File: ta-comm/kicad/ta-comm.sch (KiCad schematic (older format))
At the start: 55 parts, among them IC1 CC1110F32RHHR, IC2 F2972NEGK, IC3 RFFM6404, IC4 STA0693A, J1 Conn_01x16, J2 Conn_01x16, J3 A-1JB, J4 Conn_01x04, J5 Conn_01x04, Y1 FOX924B-27

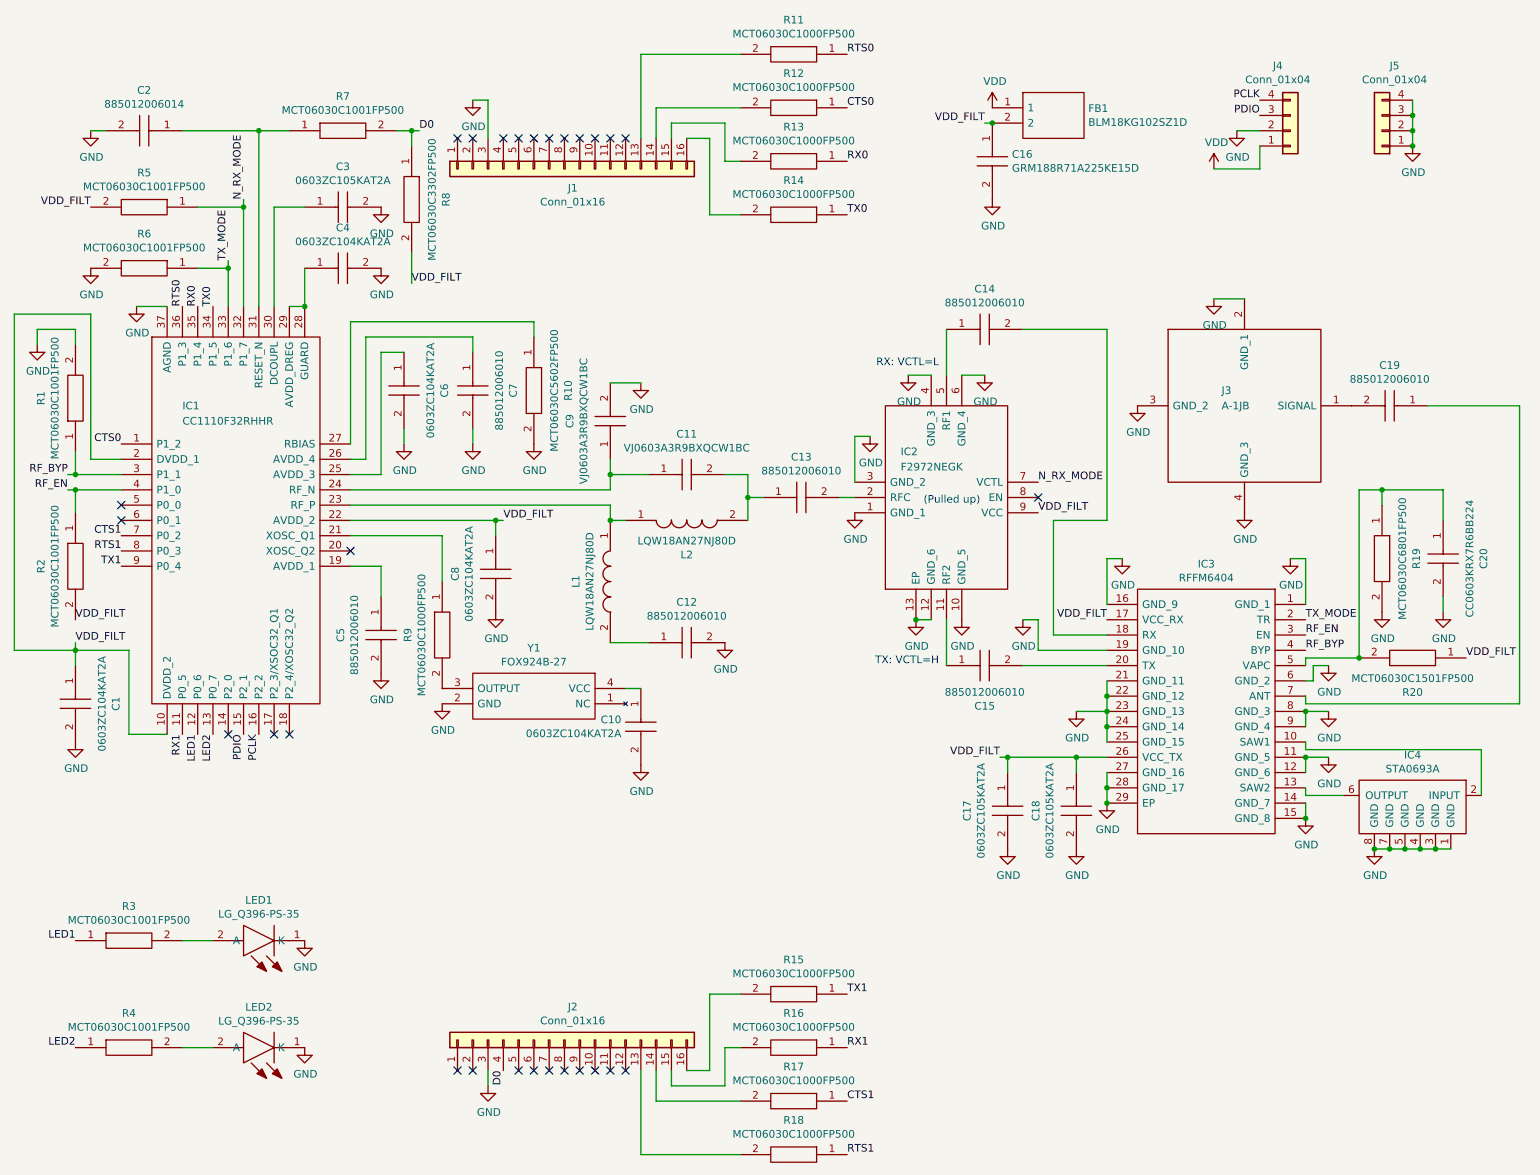
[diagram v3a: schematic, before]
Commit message: Updates communication board schematic and PCB
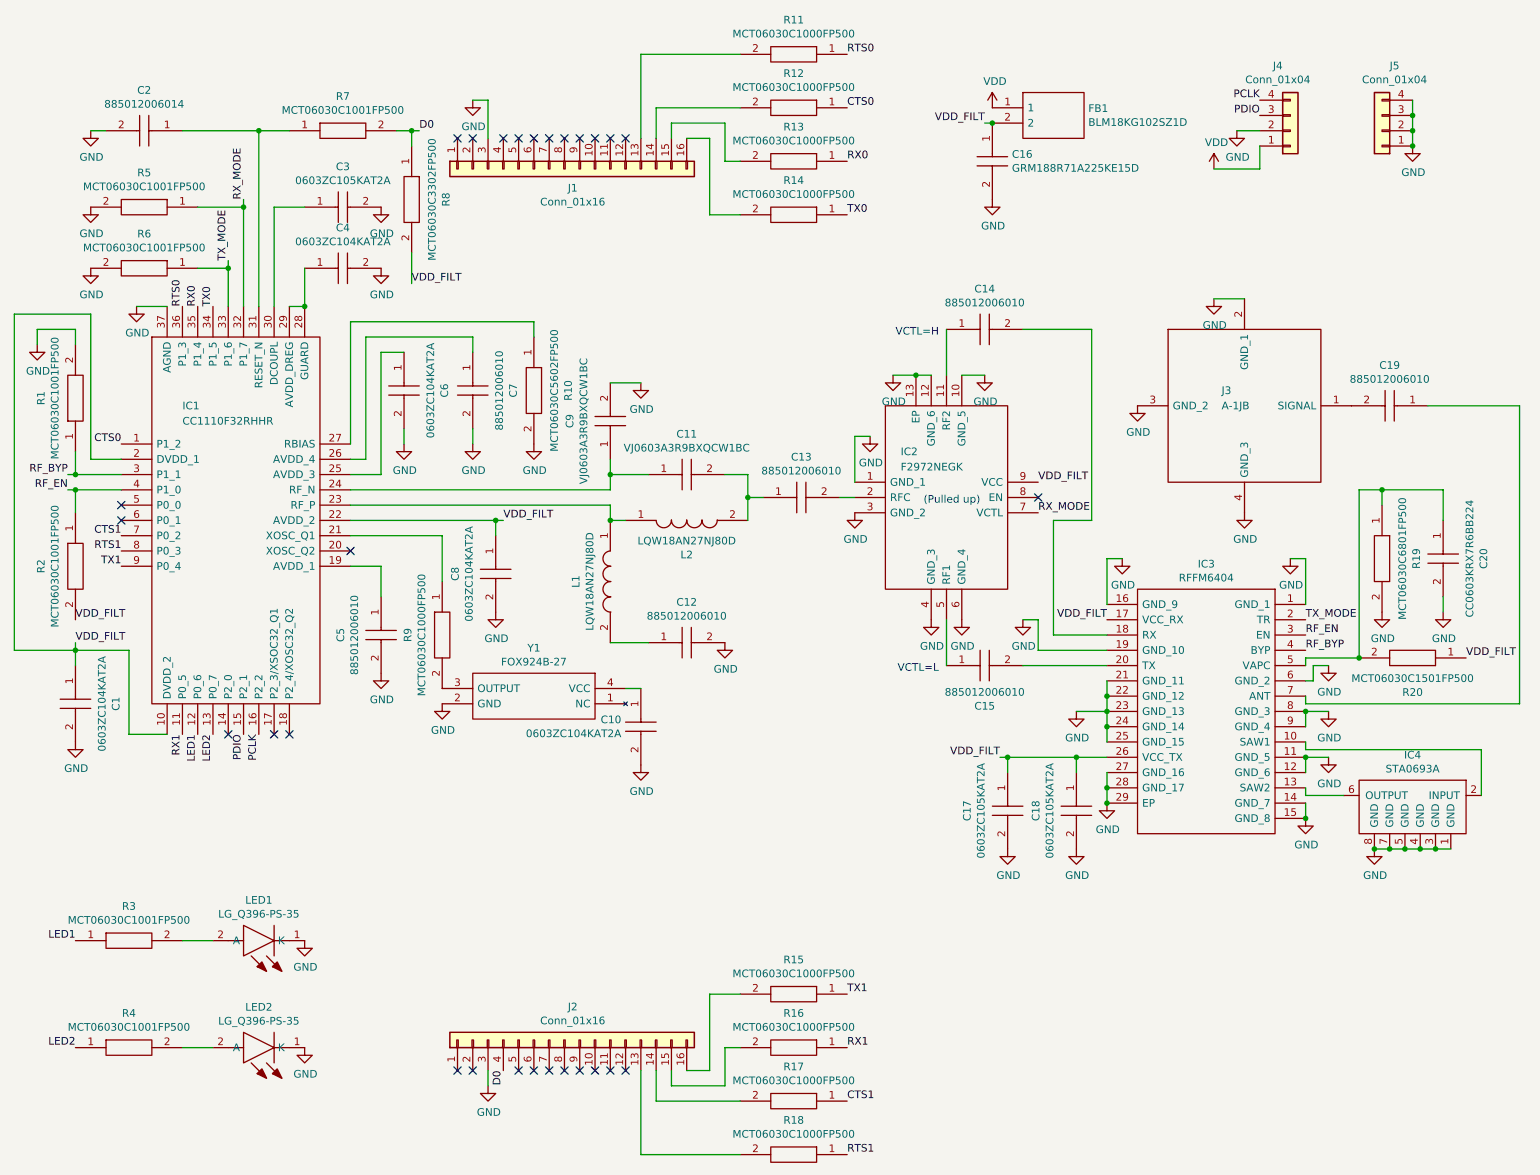
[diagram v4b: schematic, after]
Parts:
- IC2: footprint ta-comm:QFN50P200X200X55-13N-D -> QFN50P200X200X55-13N-D
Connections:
- net GND: now also R5.2
- net VDD_FILT: no longer R5.2
- net at IC2.11 (RF2): now also C14.1; no longer C15.1
- net at IC2.5 (RF1): now also C15.1; no longer C14.1
- net N_RX_MODE renamed RX_MODE
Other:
- note added: "VCTL=H"
- note added: "VCTL=L"
- note removed: "RX: VCTL=L"
- note removed: "TX: VCTL=H"
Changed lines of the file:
@@
 TX_MODE
 Text Label 2100 1700 1    50   ~ 0
-N_RX_MODE
-Wire Wire Line
-	2200 1250 2200 2400
+RX_MODE
 Wire Wire Line
 	2000 2100 2000 2150
@@
 Wire Wire Line
 	2100 1750 2100 2400
-Text Label 1100 1750 2    50   ~ 0
-VDD_FILT
 $Comp
 L power:GND #PWR03
@@
 Wire Wire Line
 	1200 1250 1100 1250
-Wire Wire Line
-	1700 1250 2200 1250
-Wire Wire Line
-	2200 1250 2400 1250
-Connection ~ 2200 1250
 Text Label 3250 1250 0    50   ~ 0
 D0
@@
 	0    -1   -1   0
 $EndComp
-Wire Wire Line
-	3100 1250 3200 1250
 $Comp
 L ta-comm:MCT06030C3302FP500 R8
@@
 	0    1    1    0
 $EndComp
-Wire Wire Line
-	3200 1350 3200 1250
-Connection ~ 3200 1250
-Wire Wire Line
-	3200 1250 3250 1250
 Wire Wire Line
 	3200 2050 3200 2250
@@
 Connection ~ 9750 1250
 Connection ~ 9750 1350
-$Comp
-L ta-comm:F2972NEGK IC2
-U 1 1 5EAC12F5
-P 6100 3750
-F 0 "IC2" H 6400 3350 50  0000 L CNN
-F 1 "F2972NEGK" H 6400 3450 50  0000 L CNN
-F 2 "ta-comm:QFN50P200X200X55-13N-D" H 7150 4250 50  0001 L CNN
-F 3 "https://www.idt.com/document/dst/f2972-datasheet" H 7150 4150 50  0001 L CNN
-F 4 "VFQFP-N 2 MM X 2MM X .5MM PITCH" H 7150 4050 50  0001 L CNN "Description"
-F 5 "0.55" H 7150 3950 50  0001 L CNN "Height"
-F 6 "IDT" H 7150 3850 50  0001 L CNN "Manufacturer_Name"
-F 7 "F2972NEGK" H 7150 3750 50  0001 L CNN "Manufacturer_Part_Number"
-F 8 "972-F2972NEGK" H 7150 3650 50  0001 L CNN "Mouser Part Number"
-F 9 "https://www.mouser.com/Search/Refine.aspx?Keyword=972-F2972NEGK" H 7150 3550 50  0001 L CNN "Mouser Price/Stock"
-	1    6100 3750
-	1    0    0    1
-$EndComp
-Wire Wire Line
-	6000 3650 6100 3650
-$Comp
-L power:GND #PWR022
-U 1 1 5ED30EF6
-P 6200 3250
-F 0 "#PWR022" H 6200 3000 50  0001 C CNN
-F 1 "GND" H 6205 3077 50  0000 C CNN
-F 2 "" H 6200 3250 50  0001 C CNN
-F 3 "" H 6200 3250 50  0001 C CNN
-	1    6200 3250
-	1    0    0    -1
-$EndComp
-Wire Wire Line
-	6100 3550 6100 3250
-Wire Wire Line
-	6100 3250 6200 3250
-$Comp
-L power:GND #PWR021
-U 1 1 5ED343CA
-P 6100 3750
-F 0 "#PWR021" H 6100 3500 50  0001 C CNN
-F 1 "GND" H 6105 3577 50  0000 C CNN
-F 2 "" H 6100 3750 50  0001 C CNN
-F 3 "" H 6100 3750 50  0001 C CNN
-	1    6100 3750
-	1    0    0    -1
-$EndComp
-$Comp
-L power:GND #PWR023
-U 1 1 5ED34940
-P 6450 2850
-F 0 "#PWR023" H 6450 2600 50  0001 C CNN
-F 1 "GND" H 6455 2677 50  0000 C CNN
-F 2 "" H 6450 2850 50  0001 C CNN
-F 3 "" H 6450 2850 50  0001 C CNN
-	1    6450 2850
-	1    0    0    -1
-$EndComp
-$Comp
-L power:GND #PWR026
-U 1 1 5ED34F35
-P 6950 2850
-F 0 "#PWR026" H 6950 2600 50  0001 C CNN
-F 1 "GND" H 6955 2677 50  0000 C CNN
-F 2 "" H 6950 2850 50  0001 C CNN
-F 3 "" H 6950 2850 50  0001 C CNN
-	1    6950 2850
-	1    0    0    -1
-$EndComp
-Wire Wire Line
-	6450 2850 6600 2850
-Wire Wire Line
-	6800 2850 6950 2850
-Wire Wire Line
-	6600 4450 6500 4450
-$Comp
-L power:GND #PWR024
-U 1 1 5ED3E019
-P 6500 4450
-F 0 "#PWR024" H 6500 4200 50  0001 C CNN
-F 1 "GND" H 6505 4277 50  0000 C CNN
-F 2 "" H 6500 4450 50  0001 C CNN
-F 3 "" H 6500 4450 50  0001 C CNN
-	1    6500 4450
-	1    0    0    -1
-$EndComp
-Connection ~ 6500 4450
-$Comp
-L power:GND #PWR025
-U 1 1 5ED3E5CB
-P 6800 4450
-F 0 "#PWR025" H 6800 4200 50  0001 C CNN
-F 1 "GND" H 6805 4277 50  0000 C CNN
-F 2 "" H 6800 4450 50  0001 C CNN
-F 3 "" H 6800 4450 50  0001 C CNN
-	1    6800 4450
-	1    0    0    -1
-$EndComp
-NoConn ~ 7300 3650
-Text Label 7300 3550 0    50   ~ 0
-N_RX_MODE
-Text Label 7300 3750 0    50   ~ 0
-VDD_FILT
-Text Notes 6550 3700 0    50   ~ 0
-(Pulled up)
 Text Label 9050 4450 0    50   ~ 0
 TX_MODE
@@
 Wire Wire Line
 	7750 4050 7850 4050
-Wire Wire Line
-	6700 2550 6700 2850
 Text Label 10100 4700 0    50   ~ 0
 VDD_FILT
@@
 Wire Wire Line
 	7400 4550 7400 3800
-Wire Wire Line
-	7400 3800 7750 3800
-Wire Wire Line
-	7750 3800 7750 2550
-Wire Wire Line
-	7750 2550 7200 2550
-Wire Wire Line
-	6700 4450 6700 4750
 Wire Wire Line
 	7200 4750 7750 4750
@@
 NoConn ~ 4500 1300
 NoConn ~ 4600 1300
-Text Notes 6650 2800 2    50   ~ 0
-RX: VCTL=L
-Text Notes 6650 4750 2    50   ~ 0
-TX: VCTL=H
+Text Notes 6650 4800 2    50   ~ 0
+VCTL=L
+Text Notes 6650 2600 2    50   ~ 0
+VCTL=H
+$Comp
+L power:GND #PWR021
+U 1 1 5E96E772
+P 1100 1750
+F 0 "#PWR021" H 1100 1500 50  0001 C CNN
+F 1 "GND" H 1105 1577 50  0000 C CNN
+F 2 "" H 1100 1750 50  0001 C CNN
+F 3 "" H 1100 1750 50  0001 C CNN
+	1    1100 1750
+	1    0    0    -1
+$EndComp
+Wire Wire Line
+	3200 1250 3250 1250
+Wire Wire Line
+	3100 1250 3200 1250
+Connection ~ 3200 1250
+Wire Wire Line
+	3200 1350 3200 1250
+Wire Wire Line
+	2200 1250 2400 1250
+Wire Wire Line
+	1700 1250 2200 1250
+Connection ~ 2200 1250
+Wire Wire Line
+	2200 1250 2200 2400
+Wire Wire Line
+	7200 2550 7650 2550
+Wire Wire Line
+	7650 2550 7650 3800
+Wire Wire Line
+	7650 3800 7400 3800
+$Comp
+L ta-comm:F2972NEGK IC2
+U 1 1 5E99286D
+P 6100 3550
+F 0 "IC2" H 6400 3750 50  0000 L CNN
+F 1 "F2972NEGK" H 6400 3650 50  0000 L CNN
+F 2 "QFN50P200X200X55-13N-D" H 7150 4050 50  0001 L CNN
+F 3 "https://www.idt.com/document/dst/f2972-datasheet" H 7150 3950 50  0001 L CNN
+F 4 "VFQFP-N 2 MM X 2MM X .5MM PITCH" H 7150 3850 50  0001 L CNN "Description"
+F 5 "0.55" H 7150 3750 50  0001 L CNN "Height"
+F 6 "IDT" H 7150 3650 50  0001 L CNN "Manufacturer_Name"
+F 7 "F2972NEGK" H 7150 3550 50  0001 L CNN "Manufacturer_Part_Number"
+F 8 "972-F2972NEGK" H 7150 3450 50  0001 L CNN "Mouser Part Number"
+F 9 "https://www.mouser.com/Search/Refine.aspx?Keyword=972-F2972NEGK" H 7150 3350 50  0001 L CNN "Mouser Price/Stock"
+	1    6100 3550
+	1    0    0    -1
+$EndComp
+Wire Wire Line
+	6700 2550 6700 2850
+Wire Wire Line
+	6700 4450 6700 4750
+$Comp
+L power:GND #PWR025
+U 1 1 5E9AAA8A
+P 6600 4450
+F 0 "#PWR025" H 6600 4200 50  0001 C CNN
+F 1 "GND" H 6605 4277 50  0000 C CNN
+F 2 "" H 6600 4450 50  0001 C CNN
+F 3 "" H 6600 4450 50  0001 C CNN
+	1    6600 4450
+	1    0    0    -1
+$EndComp
+$Comp
+L power:GND #PWR026
+U 1 1 5E9AB05C
+P 6800 4450
+F 0 "#PWR026" H 6800 4200 50  0001 C CNN
+F 1 "GND" H 6805 4277 50  0000 C CNN
+F 2 "" H 6800 4450 50  0001 C CNN
+F 3 "" H 6800 4450 50  0001 C CNN
+	1    6800 4450
+	1    0    0    -1
+$EndComp
+$Comp
+L power:GND #PWR022
+U 1 1 5E9AB653
+P 6100 3750
+F 0 "#PWR022" H 6100 3500 50  0001 C CNN
+F 1 "GND" H 6105 3577 50  0000 C CNN
+F 2 "" H 6100 3750 50  0001 C CNN
+F 3 "" H 6100 3750 50  0001 C CNN
+	1    6100 3750
+	1    0    0    -1
+$EndComp
+$Comp
+L power:GND #PWR023
+U 1 1 5E9ABC4D
+P 6200 3250
+F 0 "#PWR023" H 6200 3000 50  0001 C CNN
+F 1 "GND" H 6205 3077 50  0000 C CNN
+F 2 "" H 6200 3250 50  0001 C CNN
+F 3 "" H 6200 3250 50  0001 C CNN
+	1    6200 3250
+	1    0    0    -1
+$EndComp
+Wire Wire Line
+	6100 3550 6100 3250
+Wire Wire Line
+	6100 3250 6200 3250
+Text Label 7300 3550 0    50   ~ 0
+VDD_FILT
+Text Label 7300 3750 0    50   ~ 0
+RX_MODE
+NoConn ~ 7300 3650
+Wire Wire Line
+	6000 3650 6100 3650
+$Comp
+L power:GND #PWR024
+U 1 1 5E9C0236
+P 6350 2850
+F 0 "#PWR024" H 6350 2600 50  0001 C CNN
+F 1 "GND" H 6355 2677 50  0000 C CNN
+F 2 "" H 6350 2850 50  0001 C CNN
+F 3 "" H 6350 2850 50  0001 C CNN
+	1    6350 2850
+	1    0    0    -1
+$EndComp
+$Comp
+L power:GND #PWR049
+U 1 1 5E9C0D1F
+P 6950 2850
+F 0 "#PWR049" H 6950 2600 50  0001 C CNN
+F 1 "GND" H 6955 2677 50  0000 C CNN
+F 2 "" H 6950 2850 50  0001 C CNN
+F 3 "" H 6950 2850 50  0001 C CNN
+	1    6950 2850
+	1    0    0    -1
+$EndComp
+Wire Wire Line
+	6600 2850 6500 2850
+Wire Wire Line
+	6500 2850 6350 2850
+Connection ~ 6500 2850
+Wire Wire Line
+	6800 2850 6950 2850
+Text Notes 6550 3700 0    50   ~ 0
+(Pulled up)
 $EndSCHEMATC
